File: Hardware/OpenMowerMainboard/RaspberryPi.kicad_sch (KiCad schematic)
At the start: 10 parts, among them J21 Raspberry_Pi_2_3, J22 Conn_02x03_Odd_Even, M1 Fan, Q3 BSS138, U3 SIP32509DT

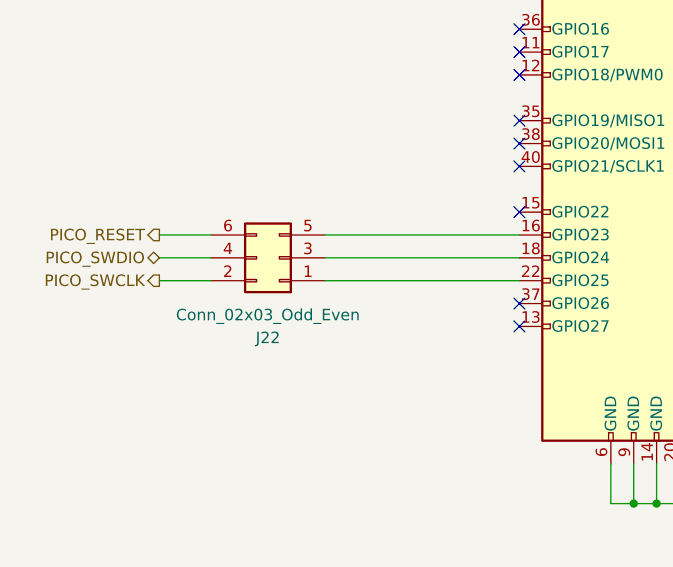
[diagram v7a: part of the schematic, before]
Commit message: v0_9_1 mainboard rework
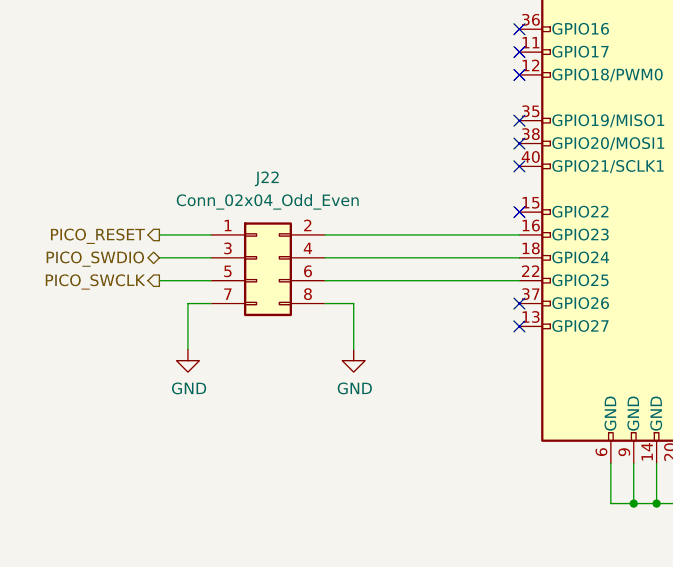
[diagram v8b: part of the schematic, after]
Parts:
- removed J22: Conn_02x03_Odd_Even, Connector_PinHeader_2.54mm:PinHeader_2x03_P2.54mm_Vertical, symbol Connector_Generic:Conn_02x03_Odd_Even
- added J22: Conn_02x04_Odd_Even, Connector_PinHeader_2.54mm:PinHeader_2x04_P2.54mm_Vertical, symbol Connector_Generic:Conn_02x04_Odd_Even
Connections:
- net GND: now also J22.7 (Pin_7), J22.8 (Pin_8)
- net PICO_RESET: now also J22.1 (Pin_1)
- net PICO_SWCLK: now also J22.5 (Pin_5)
- net PICO_SWDIO: now also J22.3 (Pin_3)
- net at J21.22 (GPIO25): now also J22.6 (Pin_6)
- net at J21.18 (GPIO24): now also J22.4 (Pin_4)
- net at J21.16 (GPIO23): now also J22.2 (Pin_2)
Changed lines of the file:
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@@
+    (stroke (width 0) (type default) (color 0 0 0 0))
+  )
+  (wire (pts (xy 52.705 149.225) (xy 50.165 149.225))
     (stroke (width 0) (type default) (color 0 0 0 0))
   )
@@
     (stroke (width 0) (type default) (color 0 0 0 0))
   )
+  (wire (pts (xy 50.165 149.225) (xy 50.165 154.305))
+    (stroke (width 0) (type default) (color 0 0 0 0))
+  )
   (wire (pts (xy 112.395 171.45) (xy 114.935 171.45))
     (stroke (width 0) (type default) (color 0 0 0 0))
@@
     (stroke (width 0) (type default) (color 0 0 0 0))
   )
+  (wire (pts (xy 65.405 149.225) (xy 68.58 149.225))
+    (stroke (width 0) (type default) (color 0 0 0 0))
+  )
   (wire (pts (xy 65.405 146.685) (xy 86.995 146.685))
     (stroke (width 0) (type default) (color 0 0 0 0))
@@
   )
   (wire (pts (xy 206.375 41.91) (xy 212.09 41.91))
+    (stroke (width 0) (type default) (color 0 0 0 0))
+  )
+  (wire (pts (xy 68.58 149.225) (xy 68.58 154.305))
     (stroke (width 0) (type default) (color 0 0 0 0))
   )
@@
     (pin "2")
   )
-  (symbol (lib_id "Connector_Generic:Conn_02x03_Odd_Even") (at 60.325 144.145 180) (unit 1)
+  (symbol (lib_id "Device:D_Schottky") (at 107.95 35.56 270) (unit 1)
     (in_bom yes) (on_board yes) (fields_autoplaced)
-    (property "Reference" "J22" (id 0) (at 59.055 153.035 0))
-    (property "Value" "Conn_02x03_Odd_Even" (id 1) (at 59.055 150.495 0))
-    (property "Footprint" "Connector_PinHeader_2.54mm:PinHeader_2x03_P2.54mm_Vertical" (id 2) (at 60.325 144.145 0)
-      (effects (font (size 1.27 1.27)) hide)
-    )
-    (property "Datasheet" "~" (id 3) (at 60.325 144.145 0)
+    (property "Reference" "D1" (id 0) (at 110.49 33.9724 90)
+      (effects (font (size 1.27 1.27)) (justify left))
+    )
+    (property "Value" "D_Schottky" (id 1) (at 110.49 36.5124 90)
+      (effects (font (size 1.27 1.27)) (justify left))
+    )
+    (property "Footprint" "Diode_SMD:D_SOD-123F" (id 2) (at 107.95 35.56 0)
+      (effects (font (size 1.27 1.27)) hide)
+    )
+    (property "Datasheet" "~" (id 3) (at 107.95 35.56 0)
+      (effects (font (size 1.27 1.27)) hide)
+    )
+    (pin "1")
+    (pin "2")
+  )
+  (symbol (lib_id "Device:R") (at 184.15 152.4 180) (unit 1)
+    (in_bom yes) (on_board yes) (fields_autoplaced)
+    (property "Reference" "R2" (id 0) (at 185.928 151.4915 0)
+      (effects (font (size 1.27 1.27)) (justify right))
+    )
+    (property "Value" "10k" (id 1) (at 185.928 154.2666 0)
+      (effects (font (size 1.27 1.27)) (justify right))
+    )
+    (property "Footprint" "Resistor_SMD:R_0805_2012Metric_Pad1.20x1.40mm_HandSolder" (id 2) (at 185.928 152.4 90)
+      (effects (font (size 1.27 1.27)) hide)
+    )
+    (property "Datasheet" "~" (id 3) (at 184.15 152.4 0)
+      (effects (font (size 1.27 1.27)) hide)
+    )
+    (pin "1")
+    (pin "2")
+  )
+  (symbol (lib_id "Connector_Generic:Conn_02x04_Odd_Even") (at 57.785 144.145 0) (unit 1)
+    (in_bom yes) (on_board yes) (fields_autoplaced)
+    (property "Reference" "J22" (id 0) (at 59.055 135.255 0))
+    (property "Value" "Conn_02x04_Odd_Even" (id 1) (at 59.055 137.795 0))
+    (property "Footprint" "Connector_PinHeader_2.54mm:PinHeader_2x04_P2.54mm_Vertical" (id 2) (at 57.785 144.145 0)
+      (effects (font (size 1.27 1.27)) hide)
+    )
+    (property "Datasheet" "~" (id 3) (at 57.785 144.145 0)
       (effects (font (size 1.27 1.27)) hide)
     )
@@
     (pin "5")
     (pin "6")
-  )
-  (symbol (lib_id "Device:D_Schottky") (at 107.95 35.56 270) (unit 1)
-    (in_bom yes) (on_board yes) (fields_autoplaced)
-    (property "Reference" "D1" (id 0) (at 110.49 33.9724 90)
-      (effects (font (size 1.27 1.27)) (justify left))
-    )
-    (property "Value" "D_Schottky" (id 1) (at 110.49 36.5124 90)
-      (effects (font (size 1.27 1.27)) (justify left))
-    )
-    (property "Footprint" "Diode_SMD:D_SOD-123F" (id 2) (at 107.95 35.56 0)
-      (effects (font (size 1.27 1.27)) hide)
-    )
-    (property "Datasheet" "~" (id 3) (at 107.95 35.56 0)
-      (effects (font (size 1.27 1.27)) hide)
-    )
-    (pin "1")
-    (pin "2")
-  )
-  (symbol (lib_id "Device:R") (at 184.15 152.4 180) (unit 1)
-    (in_bom yes) (on_board yes) (fields_autoplaced)
-    (property "Reference" "R2" (id 0) (at 185.928 151.4915 0)
-      (effects (font (size 1.27 1.27)) (justify right))
-    )
-    (property "Value" "10k" (id 1) (at 185.928 154.2666 0)
-      (effects (font (size 1.27 1.27)) (justify right))
-    )
-    (property "Footprint" "Resistor_SMD:R_0805_2012Metric_Pad1.20x1.40mm_HandSolder" (id 2) (at 185.928 152.4 90)
-      (effects (font (size 1.27 1.27)) hide)
-    )
-    (property "Datasheet" "~" (id 3) (at 184.15 152.4 0)
-      (effects (font (size 1.27 1.27)) hide)
-    )
-    (pin "1")
-    (pin "2")
+    (pin "7")
+    (pin "8")
+  )
+  (symbol (lib_id "power:GND") (at 50.165 154.305 0) (unit 1)
+    (in_bom yes) (on_board yes)
+    (property "Reference" "#PWR0157" (id 0) (at 50.165 160.655 0)
+      (effects (font (size 1.27 1.27)) hide)
+    )
+    (property "Value" "GND" (id 1) (at 50.292 158.6992 0))
+    (property "Footprint" "" (id 2) (at 50.165 154.305 0)
+      (effects (font (size 1.27 1.27)) hide)
+    )
+    (property "Datasheet" "" (id 3) (at 50.165 154.305 0)
+      (effects (font (size 1.27 1.27)) hide)
+    )
+    (pin "1")
+  )
+  (symbol (lib_id "power:GND") (at 68.58 154.305 0) (unit 1)
+    (in_bom yes) (on_board yes)
+    (property "Reference" "#PWR0173" (id 0) (at 68.58 160.655 0)
+      (effects (font (size 1.27 1.27)) hide)
+    )
+    (property "Value" "GND" (id 1) (at 68.707 158.6992 0))
+    (property "Footprint" "" (id 2) (at 68.58 154.305 0)
+      (effects (font (size 1.27 1.27)) hide)
+    )
+    (property "Datasheet" "" (id 3) (at 68.58 154.305 0)
+      (effects (font (size 1.27 1.27)) hide)
+    )
+    (pin "1")
   )
   (symbol (lib_id "power:GND") (at 106.045 171.45 0) (unit 1)
